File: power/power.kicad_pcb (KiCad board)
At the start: 2 copper layers, 66.1 x 84.5 mm, 69 parts, among them J1 Conn_01x02_Female, J10 Conn_01x02_Female, J11 Conn_01x02_Female, J12 Conn_01x02_Female, J13 Conn_01x02_Female, J14 Conn_01x02_Female, J15 Conn_01x03_Male, J2 Barrel_jack, J3 Conn_01x02_Female, J4 Conn_01x02_Female, J5 CONN_02X03, J6 Conn_01x02_Female, J7 Conn_01x02_Female, J8 Conn_01x02_Female, J9 Conn_01x02_Female, Q1 BS170, Q2 BS170, Q3 BS170, Q4 BS170, Q5 BS170, Q6 BS170, U1 ATMEGA16M1, U2 TPS2592xx, U3 LP5907MFX-3_3_NOPB

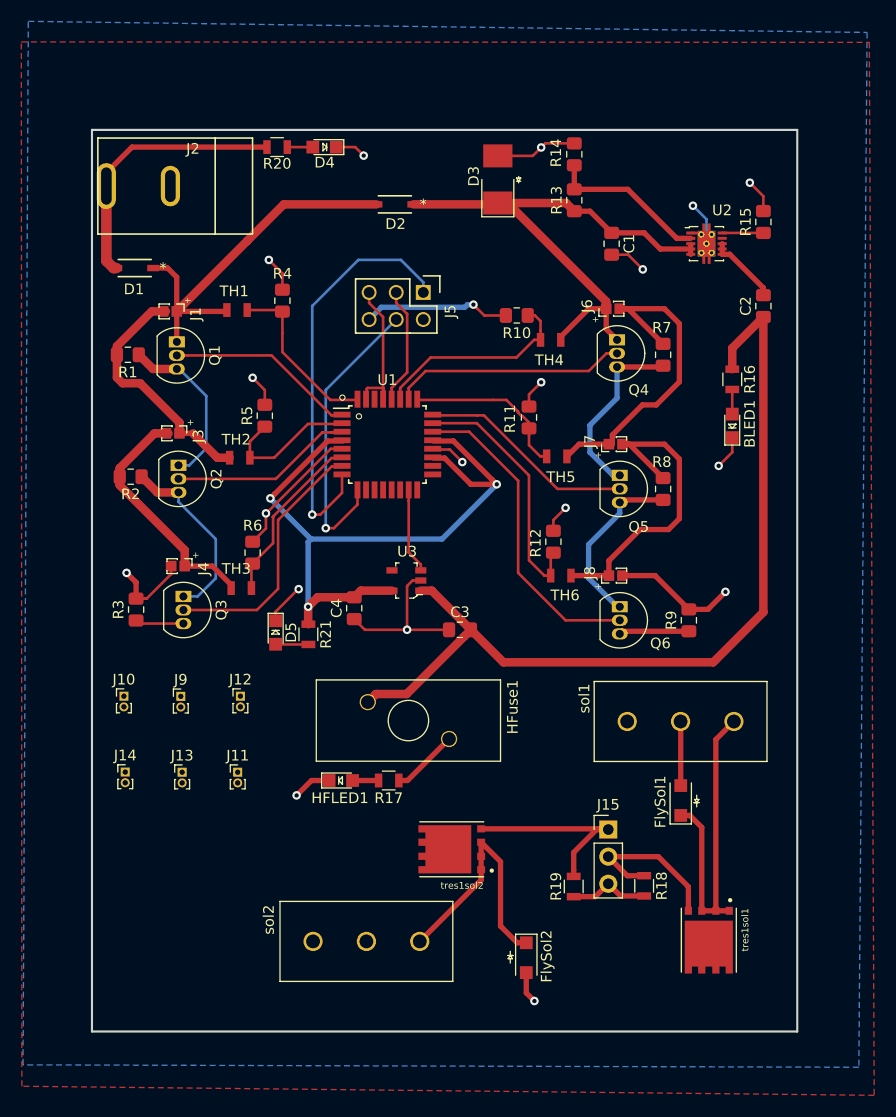
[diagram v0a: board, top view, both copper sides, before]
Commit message: complete bms - 0 drc errors, ribbon cable, pads not on edge
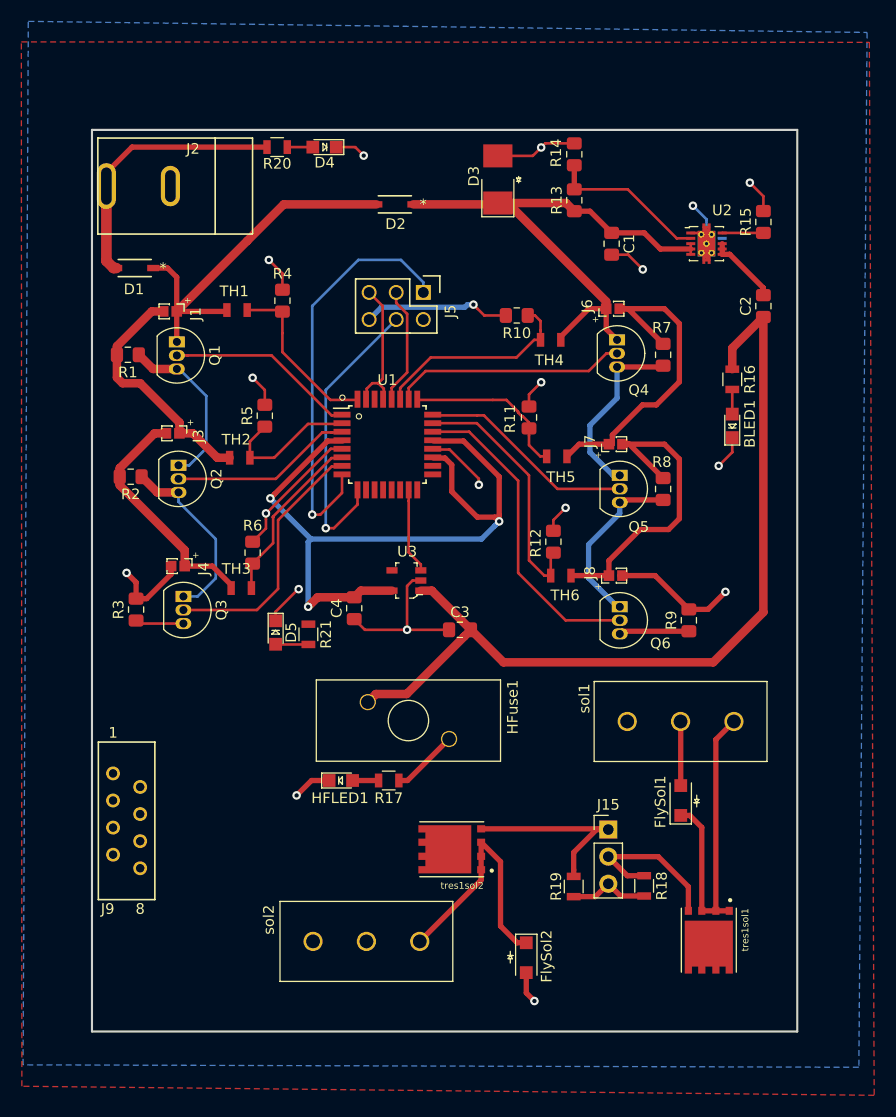
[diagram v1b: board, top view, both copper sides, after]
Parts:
- removed J10, J11, J12, J13, J14: Conn_01x02_Female, Connector_PinHeader_1.00mm:PinHeader_1x02_P1.00mm_Vertical
- J9: value Conn_01x02_Female -> MM_F_RA_08; footprint Connector_PinHeader_1.00mm:PinHeader_1x02_P1.00mm_Vertical -> footprints:micromatch_female_ra_8
- U2: footprint Package_SON:VSON-10-1EP_3x3mm_P0.5mm_EP1.65x2.4mm_ThermalVias -> footprints:VSON-10-1EP_3x3mm_P0.5mm_EP1.65x2.4mm_ThermalVias
- moved J9 13.8 mm to (133.5, 114.4)
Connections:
- J9 pad 2: GND -> +3V3
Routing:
- net GND: track 127.2 -> 134.3 mm
- net +3V3: track 65.1 -> 69.5 mm
- net /RESET: track 14.3 -> 13.3 mm
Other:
- board text added: "GND"
- board text removed: "Baro1"
- board text removed: "Baro2"
- board text removed: "GPS"
- board text removed: "IMU"
- board text removed: "Radio"
- board text removed: "Teensy"

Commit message: complete bms with list checked
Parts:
- moved sol1 23.3 mm to (187.7, 127.7), turned to 0 degrees
- moved tres1sol1 20.1 mm to (184.4, 105.5), turned to 180 degrees
- moved FlySol1 10.2 mm to (192.7, 120.1), turned to 270 degrees
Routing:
- net /12V_Switch: track 6.32 -> 40.1 mm
- net /12V_Solenoid: track 31.3 -> 40.9 mm
- net /solenoid: track 15.0 -> 21.1 mm

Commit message: screenshots
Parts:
- J1: value Conn_01x02_Female -> (none)
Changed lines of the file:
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@@
   )
   (setup
-    (last_trace_width 0.5)
+    (last_trace_width 0.25)
     (user_trace_width 0.5)
     (user_trace_width 0.8)
@@
     (pad 2 smd rect (at 0 1.27 90) (size 1 1) (layers F.Cu F.Paste F.Mask)
       (net 8 /B1B-))
-    (model ${KISYS3DMOD}/Connector_PinHeader_1.00mm.3dshapes/PinHeader_1x02_P1.00mm_Vertical.wrl
-      (at (xyz 0 0 0))
-      (scale (xyz 1 1 1))
-      (rotate (xyz 0 0 0))
-    )
   )
   (module Resistor_SMD:R_0805_2012Metric_Pad1.15x1.40mm_HandSolder (layer F.Cu)
@@
       (effects (font (size 1 1) (thickness 0.15)))
     )
-    (fp_text value LED_0805_Red (at 0.508 2.032 180) (layer F.Fab) hide
+    (fp_text value LED_0805_Red (at -9.131034 0.346542 180) (layer F.Fab) hide
       (effects (font (size 1 1) (thickness 0.15)))
     )
@@
       (effects (font (size 1 1) (thickness 0.15)))
     )
-    (fp_text value OSTTC03 (at 15.24 -9.39 180) (layer F.Fab) hide
+    (fp_text value OSTTC03 (at 16.002 -7.239 180) (layer F.Fab) hide
       (effects (font (size 1 1) (thickness 0.15)))
     )
@@
       (effects (font (size 1 1) (thickness 0.15)))
     )
-    (fp_text value Conn_01x02_Female (at 0 3.048 270) (layer F.Fab) hide
+    (fp_text value "" (at 0 3.048 270) (layer F.Fab) hide
       (effects (font (size 1 1) (thickness 0.15)))
     )
@@
     (pad 1 smd rect (at 0 0 270) (size 1 1) (layers F.Cu F.Paste F.Mask)
       (net 10 /B1A+))
-    (model ${KISYS3DMOD}/Connector_PinHeader_1.00mm.3dshapes/PinHeader_1x02_P1.00mm_Vertical.wrl
-      (at (xyz 0 0 0))
-      (scale (xyz 1 1 1))
-      (rotate (xyz 0 0 0))
-    )
   )
   (module footprints:nickle_pads_1x2 (layer F.Cu)
@@
     (pad 2 smd rect (at 0 1.27 270) (size 1 1) (layers F.Cu F.Paste F.Mask)
       (net 7 /B2A-))
-    (model ${KISYS3DMOD}/Connector_PinHeader_1.00mm.3dshapes/PinHeader_1x02_P1.00mm_Vertical.wrl
-      (at (xyz 0 0 0))
-      (scale (xyz 1 1 1))
-      (rotate (xyz 0 0 0))
-    )
   )
   (module footprints:nickle_pads_1x2 (layer F.Cu)
@@
     (pad 1 smd rect (at 0 0 270) (size 1 1) (layers F.Cu F.Paste F.Mask)
       (net 7 /B2A-))
-    (model ${KISYS3DMOD}/Connector_PinHeader_1.00mm.3dshapes/PinHeader_1x02_P1.00mm_Vertical.wrl
-      (at (xyz 0 0 0))
-      (scale (xyz 1 1 1))
-      (rotate (xyz 0 0 0))
-    )
   )
   (module footprints:nickle_pads_1x2 (layer F.Cu)
@@
     (pad 2 smd rect (at 0 1.27 90) (size 1 1) (layers F.Cu F.Paste F.Mask)
       (net 9 /B2B-))
-    (model ${KISYS3DMOD}/Connector_PinHeader_1.00mm.3dshapes/PinHeader_1x02_P1.00mm_Vertical.wrl
-      (at (xyz 0 0 0))
-      (scale (xyz 1 1 1))
-      (rotate (xyz 0 0 0))
-    )
   )
   (module footprints:nickle_pads_1x2 (layer F.Cu)
@@
     (pad 1 smd rect (at 0 0 90) (size 1 1) (layers F.Cu F.Paste F.Mask)
       (net 9 /B2B-))
-    (model ${KISYS3DMOD}/Connector_PinHeader_1.00mm.3dshapes/PinHeader_1x02_P1.00mm_Vertical.wrl
-      (at (xyz 0 0 0))
-      (scale (xyz 1 1 1))
-      (rotate (xyz 0 0 0))
-    )
   )
   (module footprints:VSON-10-1EP_3x3mm_P0.5mm_EP1.65x2.4mm_ThermalVias (layer F.Cu)
